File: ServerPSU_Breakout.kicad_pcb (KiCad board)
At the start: 2 copper layers, 120 x 90 mm, 83 parts, among them J1 Conn_01x05, J2 Conn_01x14, J3 Conn_01x01, J4 Conn_01x01, J5 Conn_02x04_Odd_Even, J6 Conn_02x03_Odd_Even, Q1 DMG2302U, SW1 SW_DIP_x03, U1 LMR14206, U2 STM32F072RBTx, U3 4051, U4 MIC1555-YM5, U6 MCP1415, U7 AZ1117-3.3

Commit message: save
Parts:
- removed J5: Conn_02x04_Odd_Even, Connector_PinHeader_2.54mm:PinHeader_2x04_P2.54mm_Vertical
- removed J6: Conn_02x03_Odd_Even, Connector_PinHeader_2.54mm:PinHeader_2x03_P2.54mm_Vertical
- removed the REF** at (121.2, 64.9)
- removed the REF** at (121.2, 108.3)
- removed the REF** at (215.6, 86.2)
- removed the REF** at (107.6, 86.2)
- removed the REF** at (200.3, 130.8)
- removed the REF** at (123.1, 130.7)
- removed the REF** at (200.4, 52.8)
- removed the REF** at (123.1, 52.7)
- removed TP10: TestPoint, TestPoint:TestPoint_Pad_1.0x1.0mm
- added REF**: MountingHole_6.4mm_M6_Pad_Via, MountingHole:MountingHole_6.4mm_M6_Pad_Via, F.Cu at (215.6, 86.2)
- added REF**: MountingHole_6.4mm_M6_Pad_Via, MountingHole:MountingHole_6.4mm_M6_Pad_Via, F.Cu at (107.6, 86.2)
- added REF**: MountingHole_6.4mm_M6_Pad_Via, MountingHole:MountingHole_6.4mm_M6_Pad_Via, F.Cu at (122.9, 133.4)
- added REF**: MountingHole_6.4mm_M6_Pad_Via, MountingHole:MountingHole_6.4mm_M6_Pad_Via, F.Cu at (200.2, 133.4)
- added REF**: MountingHole_6.4mm_M6_Pad_Via, MountingHole:MountingHole_6.4mm_M6_Pad_Via, F.Cu at (200.5, 52.2)
- added REF**: MountingHole_6.4mm_M6_Pad_Via, MountingHole:MountingHole_6.4mm_M6_Pad_Via, F.Cu at (123.1, 52.2)
- added SW2: SW_DIP_x04, Button_Switch_SMD:SW_DIP_SPSTx04_Slide_6.7x11.72mm_W8.61mm_P2.54mm_LowProfile, F.Cu at (110.7, 124.1)
- added SW3: SW_DIP_x03, Button_Switch_SMD:SW_DIP_SPSTx03_Slide_6.7x9.18mm_W8.61mm_P2.54mm_LowProfile, F.Cu at (110.6, 72.0)
- added TP24: TestPoint, TestPoint:TestPoint_Pad_1.0x1.0mm, F.Cu at (105.9, 116.7)
- J2: footprint Connector_PinHeader_2.54mm:PinHeader_1x14_P2.54mm_Vertical -> ILI9341_TFTLCD:ILI9341_ResitiveTouch_TFTLCD_2.8inch_85mm_50mm
- R6, R7, R8, SW1: moved to F.Cu
- moved R8 34.1 mm to (105.2, 110.0), turned to 270 degrees
- moved R7 30.2 mm to (108.5, 110.0), turned to 270 degrees
- moved R6 26.2 mm to (111.8, 110.0), turned to 270 degrees
- moved TP9 25.9 mm to (109.2, 59.7)
- moved R13 21.3 mm to (132.7, 73.4), turned to 0 degrees
- moved R15 18.2 mm to (132.7, 75.9), turned to 0 degrees
- moved R11 18.1 mm to (118.4, 74.8), turned to 180 degrees
- moved SW1 17.5 mm to (110.7, 99.9), turned to 0 degrees
- moved J2 16.4 mm to (203.3, 86.2)
- moved R16 15.8 mm to (132.7, 78.5), turned to 0 degrees
- moved R10 15.3 mm to (118.4, 76.8), turned to 180 degrees
- moved R14 14.7 mm to (132.7, 81.0), turned to 0 degrees
- moved TP22 14.0 mm to (109.2, 52.1)
- moved TP23 14.0 mm to (109.2, 57.1)
- moved J1 14.0 mm to (111.8, 49.5)
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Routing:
- net /HighVoltageControl/MCU_3V3: track 198.0 -> 262.0 mm
- net Net-(SW2-Pad5): track 16.8 -> 66.1 mm, vias 0 -> 1
- net /MCU/SWDIO: track 57.0 -> 97.3 mm
- net Net-(R6-Pad2): track 21.3 -> 49.5 mm, vias 0 -> 2
- net /PSUConnector/PSU_ADDR0: track 84.5 -> 110.4 mm
- net Net-(SW3-Pad1): track 4.98 -> 25.3 mm, vias 0 -> 1
- net /MCU/NRST: track 97.8 -> 78.5 mm
- net /MCU/SWCLK: track 55.2 -> 74.4 mm
- net Net-(SW3-Pad2): track 6.92 -> 23.5 mm, vias 0 -> 1
- net GNDS: track 61.8 -> 76.7 mm, vias 19 -> 23
- net Net-(SW3-Pad3): track 7.93 -> 22.4 mm, vias 0 -> 1
- net /PSUConnector/PSU_ADDR2: track 99.5 -> 86.0 mm
- net Net-(R7-Pad2): track 22.0 -> 33.5 mm, vias 0 -> 2
- net Net-(R8-Pad2): track 19.3 -> 29.0 mm, vias 0 -> 2
- net /PSUConnector/PSU_ADDR1: track 96.1 -> 102.0 mm
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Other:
- board size 120 x 90 mm -> 124 x 100 mm
- board text added: "3BIT"
- board text added: "3BIT ADDR"
- board text added: "ADDR MODE"
- board text added: "ANALOG"
- board text added: "ANALOG ADDR"
- board text added: "BYPASS"
- board text added: "CommonSlot"
- board text added: "PSU Controller"
- board text added: "RevA 07/20"
- board text removed: "HPE CommonSlot PSU Controller RevA 07/20"

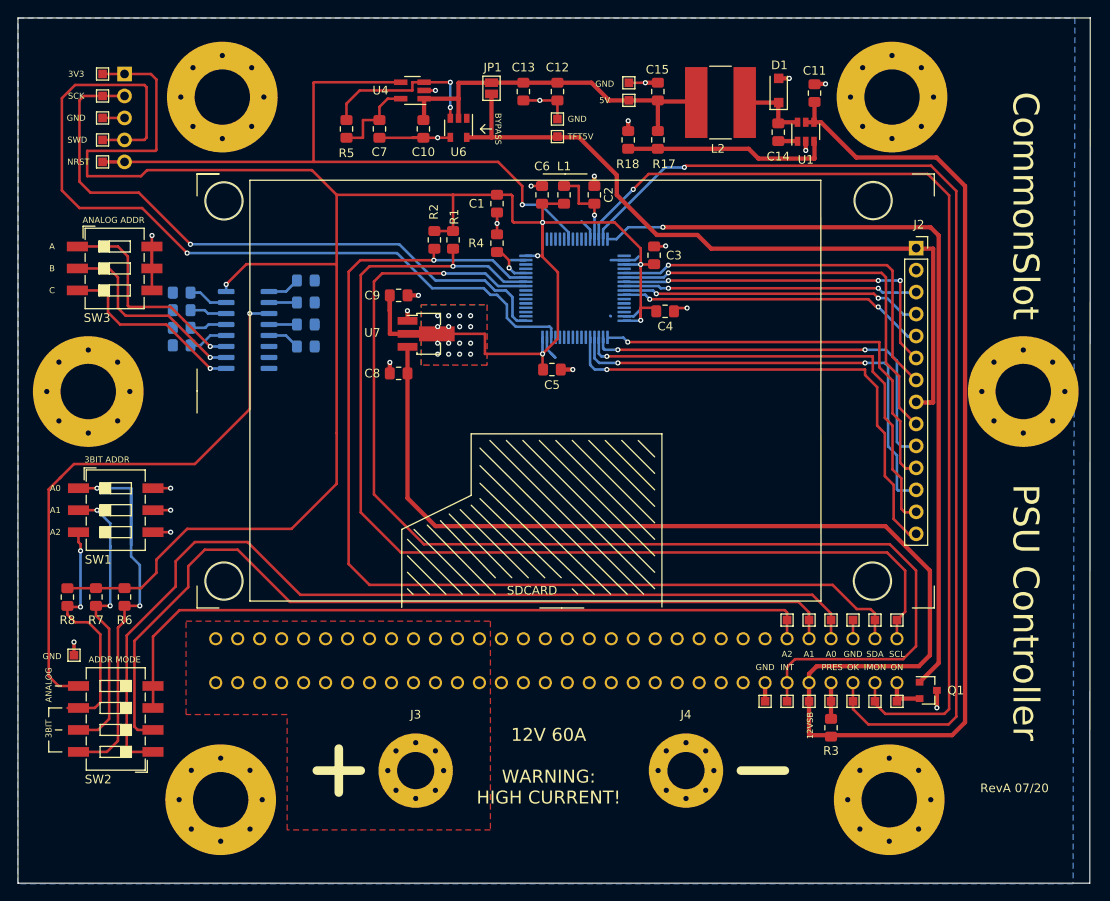
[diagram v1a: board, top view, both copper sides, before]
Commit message: Corrected Pin numbering errors :)
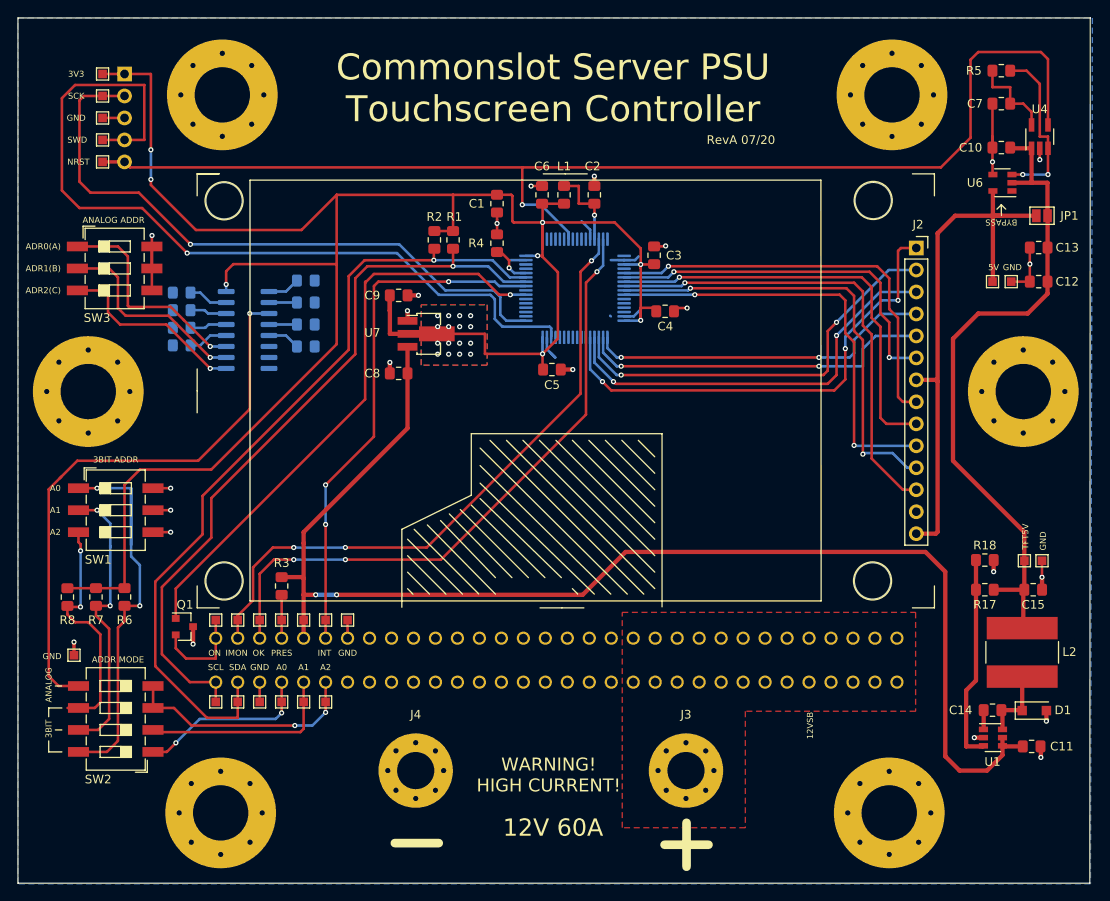
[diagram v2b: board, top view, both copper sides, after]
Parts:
- removed the REF** at (122.9, 133.4)
- removed the REF** at (200.2, 133.4)
- removed the REF** at (200.5, 52.2)
- added REF**: MountingHole_6.4mm_M6_Pad_Via, MountingHole:MountingHole_6.4mm_M6_Pad_Via, F.Cu at (122.9, 134.9)
- added REF**: MountingHole_6.4mm_M6_Pad_Via, MountingHole:MountingHole_6.4mm_M6_Pad_Via, F.Cu at (200.2, 134.9)
- added REF**: MountingHole_6.4mm_M6_Pad_Via, MountingHole:MountingHole_6.4mm_M6_Pad_Via, F.Cu at (200.5, 51.9)
- J2: footprint ILI9341_TFTLCD:ILI9341_ResitiveTouch_TFTLCD_2.8inch_85mm_50mm -> ILI9341_TFTLCD:ILI9341_ResitiveTouch_TFTLCD_2.8inch_85mm_50mm_FrontMount
- moved Q1 86.3 mm to (118.7, 113.4)
- moved C11 79.6 mm to (216.6, 127.3), turned to 0 degrees
- moved TP15 79.3 mm to (122.3, 122.1), turned to 180 degrees
- moved TP18 79.3 mm to (122.3, 112.6), turned to 180 degrees
- moved D1 77.5 mm to (216.9, 123.1), turned to 0 degrees
- moved R5 76.0 mm to (213.1, 49.1), turned to 0 degrees
- moved TP14 74.3 mm to (124.8, 122.1), turned to 180 degrees
- moved TP19 74.3 mm to (124.8, 112.6), turned to 180 degrees
- moved U1 73.3 mm to (212.1, 126.2), turned to 0 degrees
- moved TP6 73.0 mm to (217.8, 105.8), turned to 0 degrees
- moved U4 72.7 mm to (217.6, 56.8), turned to 90 degrees
- moved L2 72.5 mm to (215.5, 116.4), turned to 90 degrees
- moved C15 72.1 mm to (216.8, 109.1), turned to 180 degrees
- moved C7 71.9 mm to (213.1, 53.0), turned to 0 degrees
- moved C14 71.2 mm to (212.1, 123.1), turned to 180 degrees
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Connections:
- U2 pad 16: /HighVoltageControl/MCU_SW_IN -> Net-(U2-Pad16)
- U2 pad 55: Net-(U2-Pad55) -> /HighVoltageControl/MCU_SW_IN
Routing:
- net /PSUConnector/PSU_ADDR0: track 110.4 -> 20.3 mm, vias 0 -> 2
- net /PSUConnector/PSU_ADDR1: track 102.0 -> 23.1 mm
- net /PSUConnector/PSU_INT: track 138.1 -> 61.0 mm, vias 1 -> 3
- net /HighVoltageControl/PSU_12VSB: track 217.4 -> 152.0 mm, vias 0 -> 2
- net /MCU/NRST: track 78.5 -> 140.1 mm
- net /PSUConnector/PSU_ADDR2: track 86.0 -> 27.5 mm, vias 0 -> 2
- net /MCU/MCU_PSOK: track 123.1 -> 73.9 mm, vias 1 -> 3
- net /MCU/MCU_IMON: track 116.8 -> 73.8 mm, vias 1 -> 3
- net /PSUConnector/PSU_SCL: track 123.7 -> 85.6 mm
- net /MCU/TFTRST_5V: track 42.5 -> 76.9 mm
- net /PSUConnector/PSU_SDA: track 123.1 -> 93.9 mm
- net /HighVoltageControl/MCU_SW_IN: track 91.9 -> 68.1 mm
- net /MCU/TFT_DelayedReset/TFT_VDD_OUT: track 85.4 -> 63.4 mm
- net /MCU/TFT_CS: track 34.1 -> 54.6 mm, vias 2 -> 1
- net /MCU/TFT_RST: track 34.9 -> 52.7 mm
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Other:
- board text added: "12V 60A"
- board text added: "ADR0(A)"
- board text added: "ADR1(B)"
- board text added: "ADR2(C)"
- board text added: "Commonslot Server PSU Touchscreen Controller"
- board text added: "JLCJLCJLCJLC"
- board text added: "WARNING! HIGH CURRENT!"
- board text removed: "12V 60A WARNING: HIGH CURRENT!"
- board text removed: "B"
- board text removed: "C"
- board text removed: "CommonSlot"
- board text removed: "HPE MODE"
- board text removed: "MURATA MODE"
- board text removed: "PSU Controller"
